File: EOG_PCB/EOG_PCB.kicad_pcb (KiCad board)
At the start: 2 copper layers, 100.3 x 101.6 mm, 38 parts, among them J1 POWER OUT, J2 POWER IN, J3 SIGNAL INPUT, J4 OUT, U1 LM7805_TO220, U2 LM7905_TO220, U3 INA114AP, U4 TL082, U5 TL082, U6 TL082

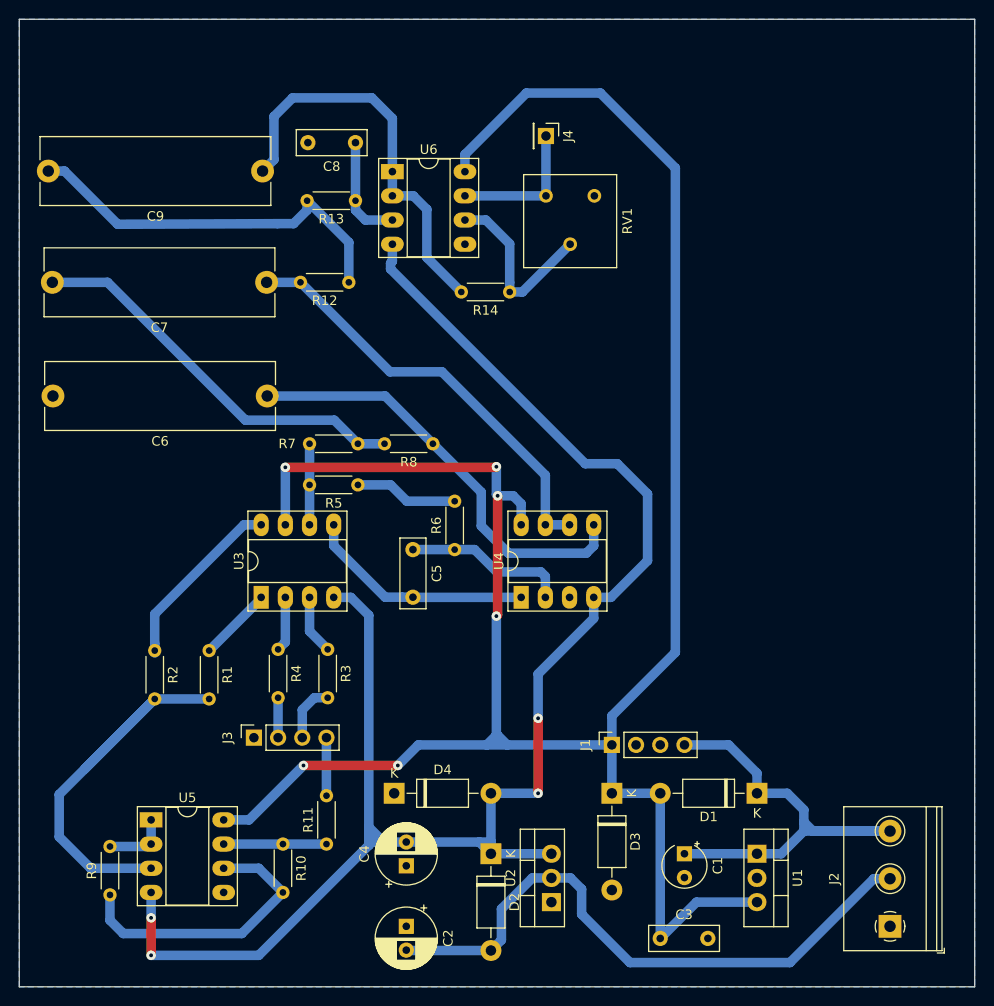
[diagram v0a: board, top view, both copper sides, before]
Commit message: Layout Improvements & Added B-CU, Label pdf files
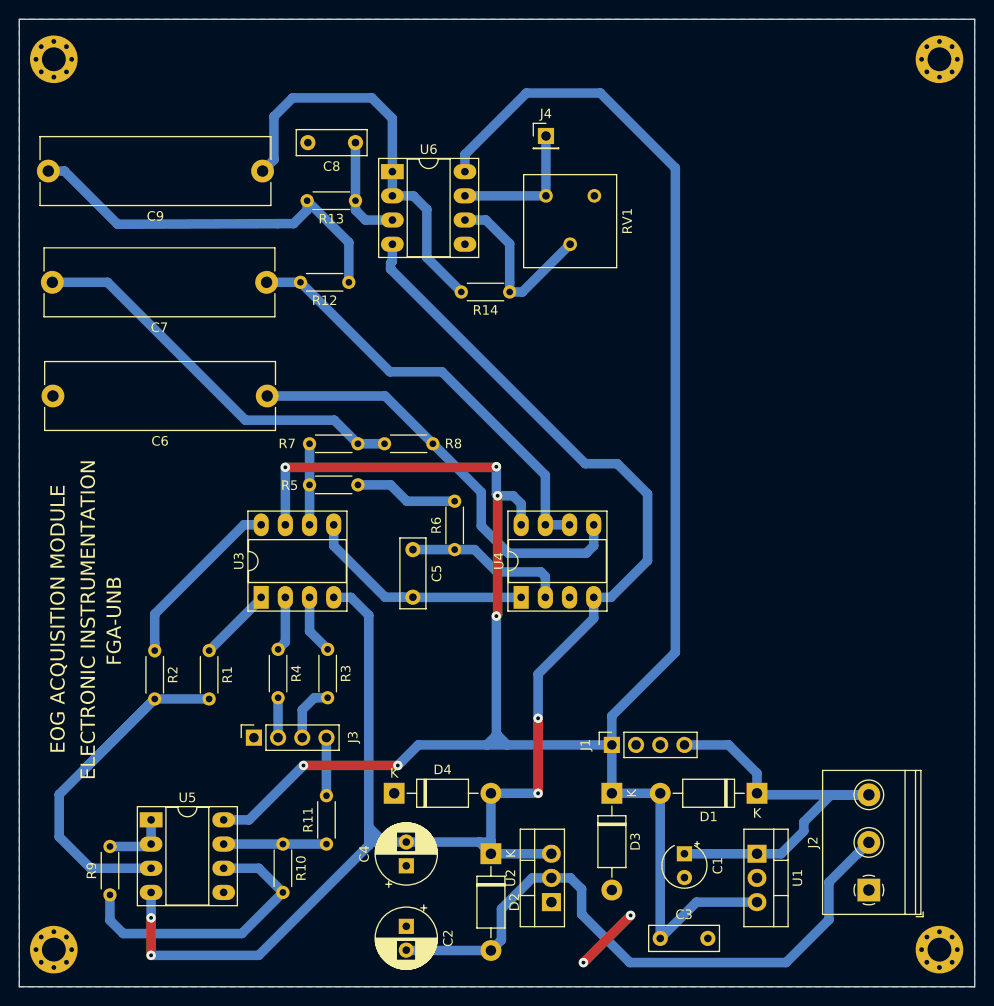
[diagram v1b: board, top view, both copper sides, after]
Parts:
- added REF**: MountingHole_2.5mm_Pad_Via, MountingHole:MountingHole_2.5mm_Pad_Via, F.Cu at (263.0, 148.5)
- added REF**: MountingHole_2.5mm_Pad_Via, MountingHole:MountingHole_2.5mm_Pad_Via, F.Cu at (170.0, 148.5)
- added REF**: MountingHole_2.5mm_Pad_Via, MountingHole:MountingHole_2.5mm_Pad_Via, F.Cu at (263.0, 55.0)
- added REF**: MountingHole_2.5mm_Pad_Via, MountingHole:MountingHole_2.5mm_Pad_Via, F.Cu at (170.0, 55.0)
- moved J2 4.41 mm to (255.6, 142.2)
- turned J4 to 0 degrees
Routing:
- net GND: track 0.00 -> 7.13 mm, vias 0 -> 2
- net +9V: track 50.8 -> 45.3 mm
- net -9V: track 64.8 -> 66.4 mm
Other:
- board text added: "ELECTRONIC INSTRUMENTATION"
- board text added: "EOG ACQUISITION MODULE"
- board text added: "FGA-UNB"
